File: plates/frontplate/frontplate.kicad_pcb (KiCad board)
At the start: 2 copper layers, 33.2 x 78.4 mm, 2 parts

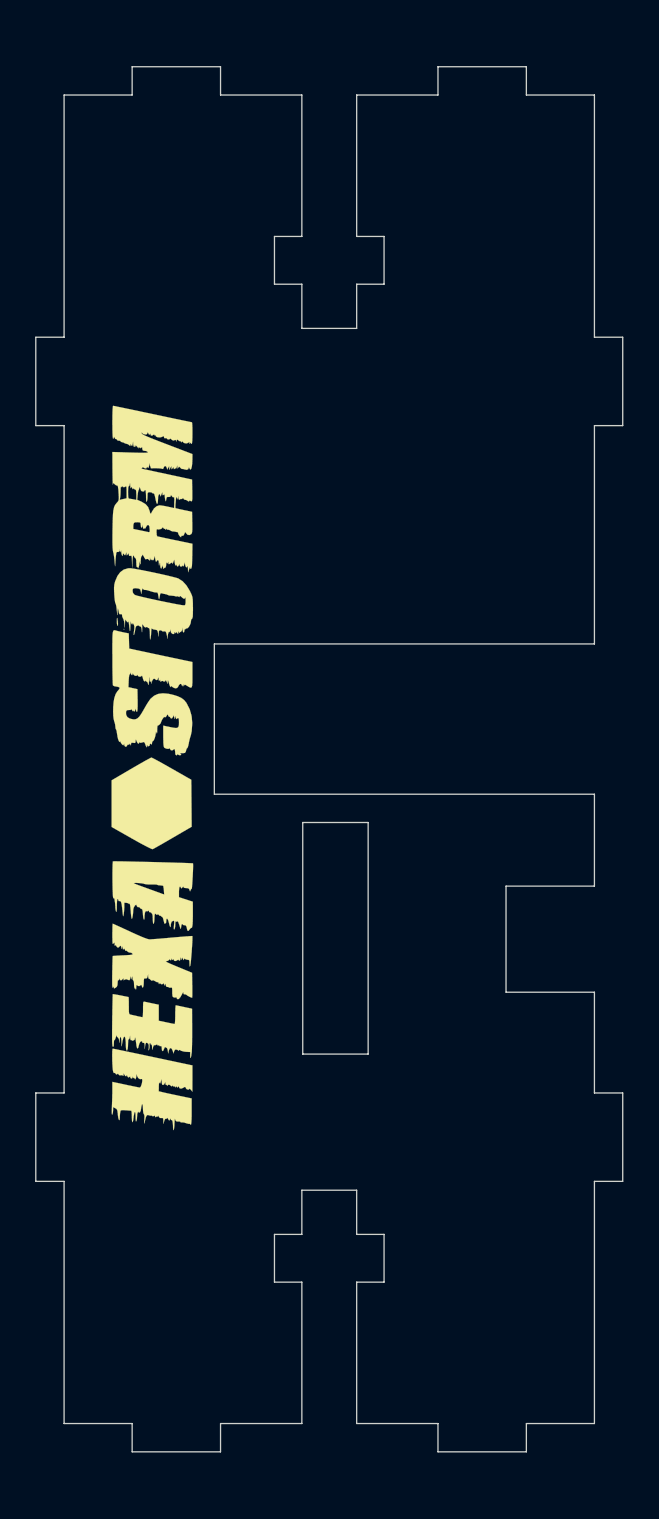
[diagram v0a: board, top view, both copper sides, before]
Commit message: improved bom changed export settings
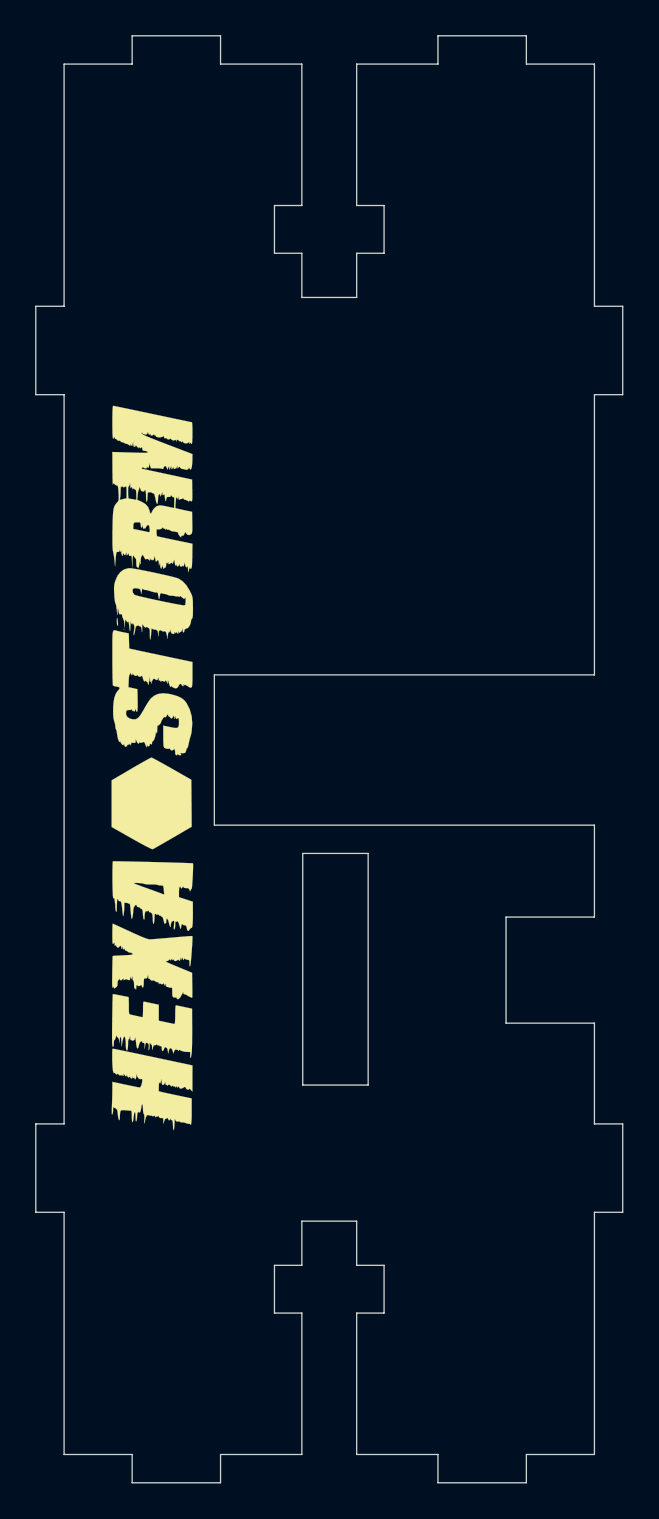
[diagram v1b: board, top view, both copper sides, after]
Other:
- board size 33.2 x 78.4 mm -> 33.2 x 81.9 mm

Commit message: added design of june
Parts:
- moved L2 4.29 mm to (148.2, 104.1)
- moved L1 4.17 mm to (148.2, 105.1)
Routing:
- net (no net): vias 0 -> 2
- added copper zone on B.Cu, net (none)
- added copper zone on F.Cu, net (none)
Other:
- board size 33.2 x 81.9 mm -> 25.2 x 55.1 mm
- net class Default removed
- board text added: "HEXASTORM"
